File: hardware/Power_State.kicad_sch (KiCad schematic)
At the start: 27 parts, among them J12 Battery_Meas, J13 ICSP_Header_2, J14 5V_In, J15 Stat_LED, J16 ICSP_Header_1, J17 Button_Header, J18 RPI_POWER, Q2 AOD4184A, SW1 SW_DIP_x01, SW2 SW_Reset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

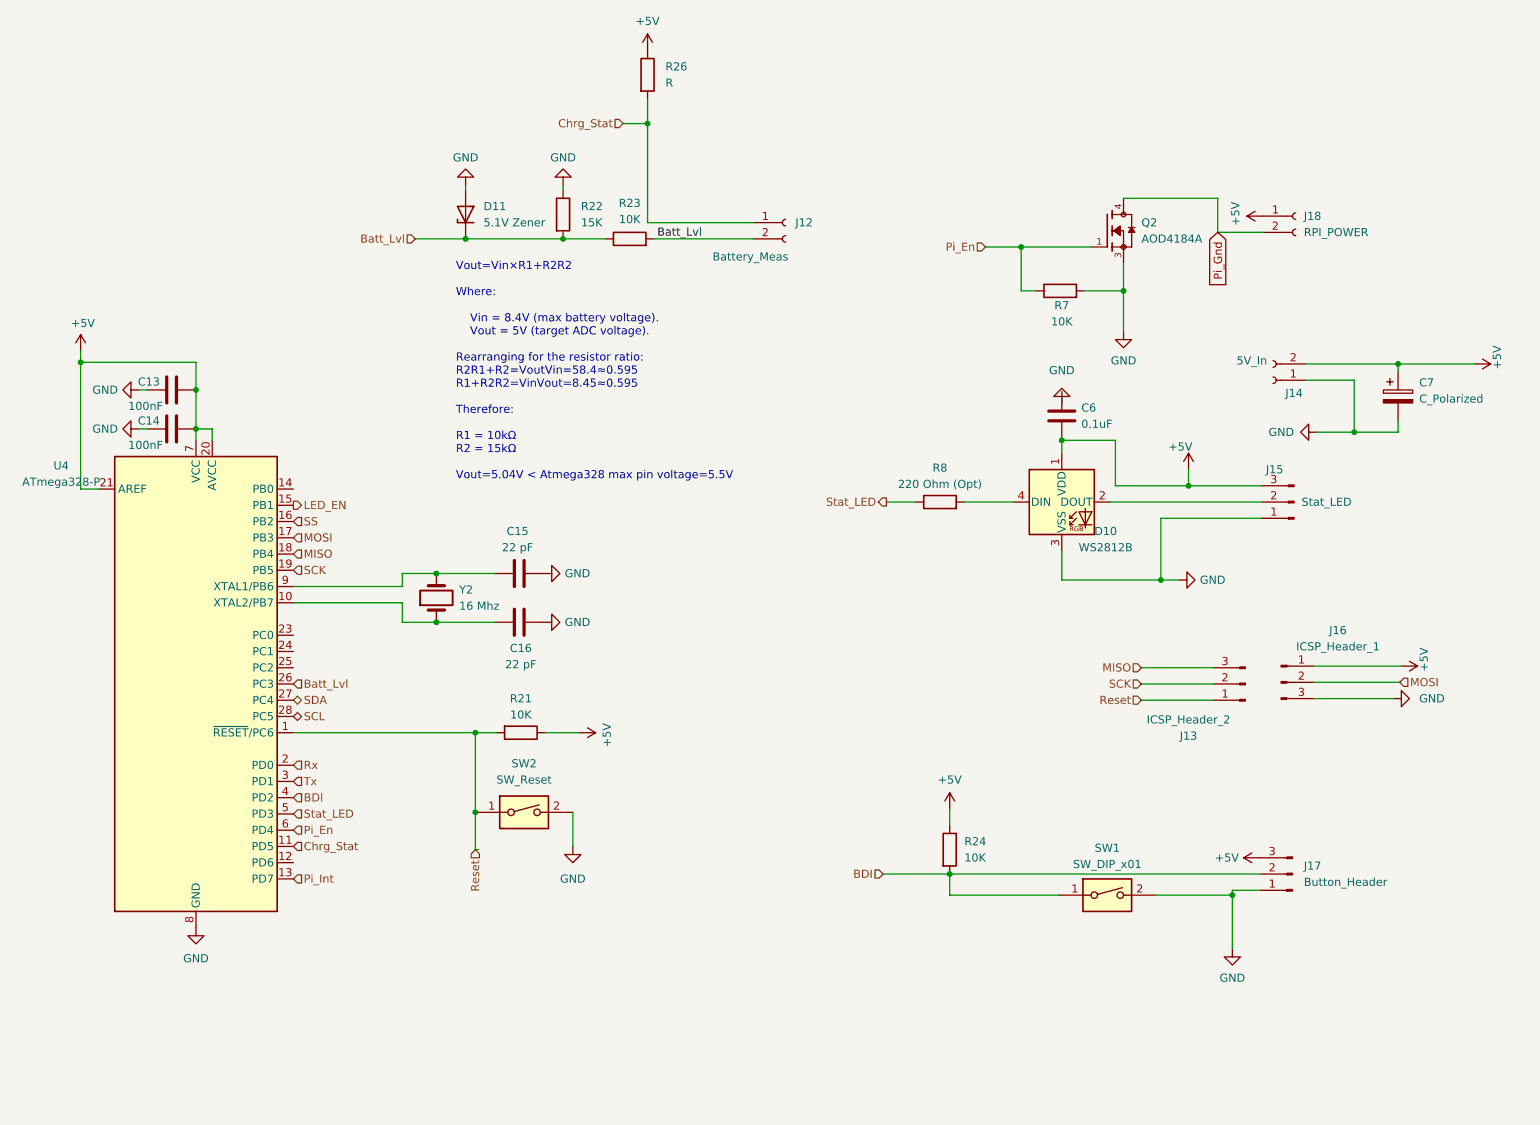
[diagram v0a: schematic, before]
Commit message: Hardware V0.2 - Schematics update
Combines Cell holder, BMS, and voltage regulator into single board
complete w. extensive electrical and thermal protections including:

* MM3220 BMS w Overvoltage, Overcurrent, undervoltage charging/discharge protect
* Fuses on cells, 12v in, 5v and 8.4v out.
* Reverse polarity protection on 12v and cells.

Adds debug UART header
Single IO header on every board
Minor component size corrections
Add current limiting resistor to RPI power NMOS gate.
Add optional support for MLCC/tantalum caps for Voltage Regulator instead of electrolytic
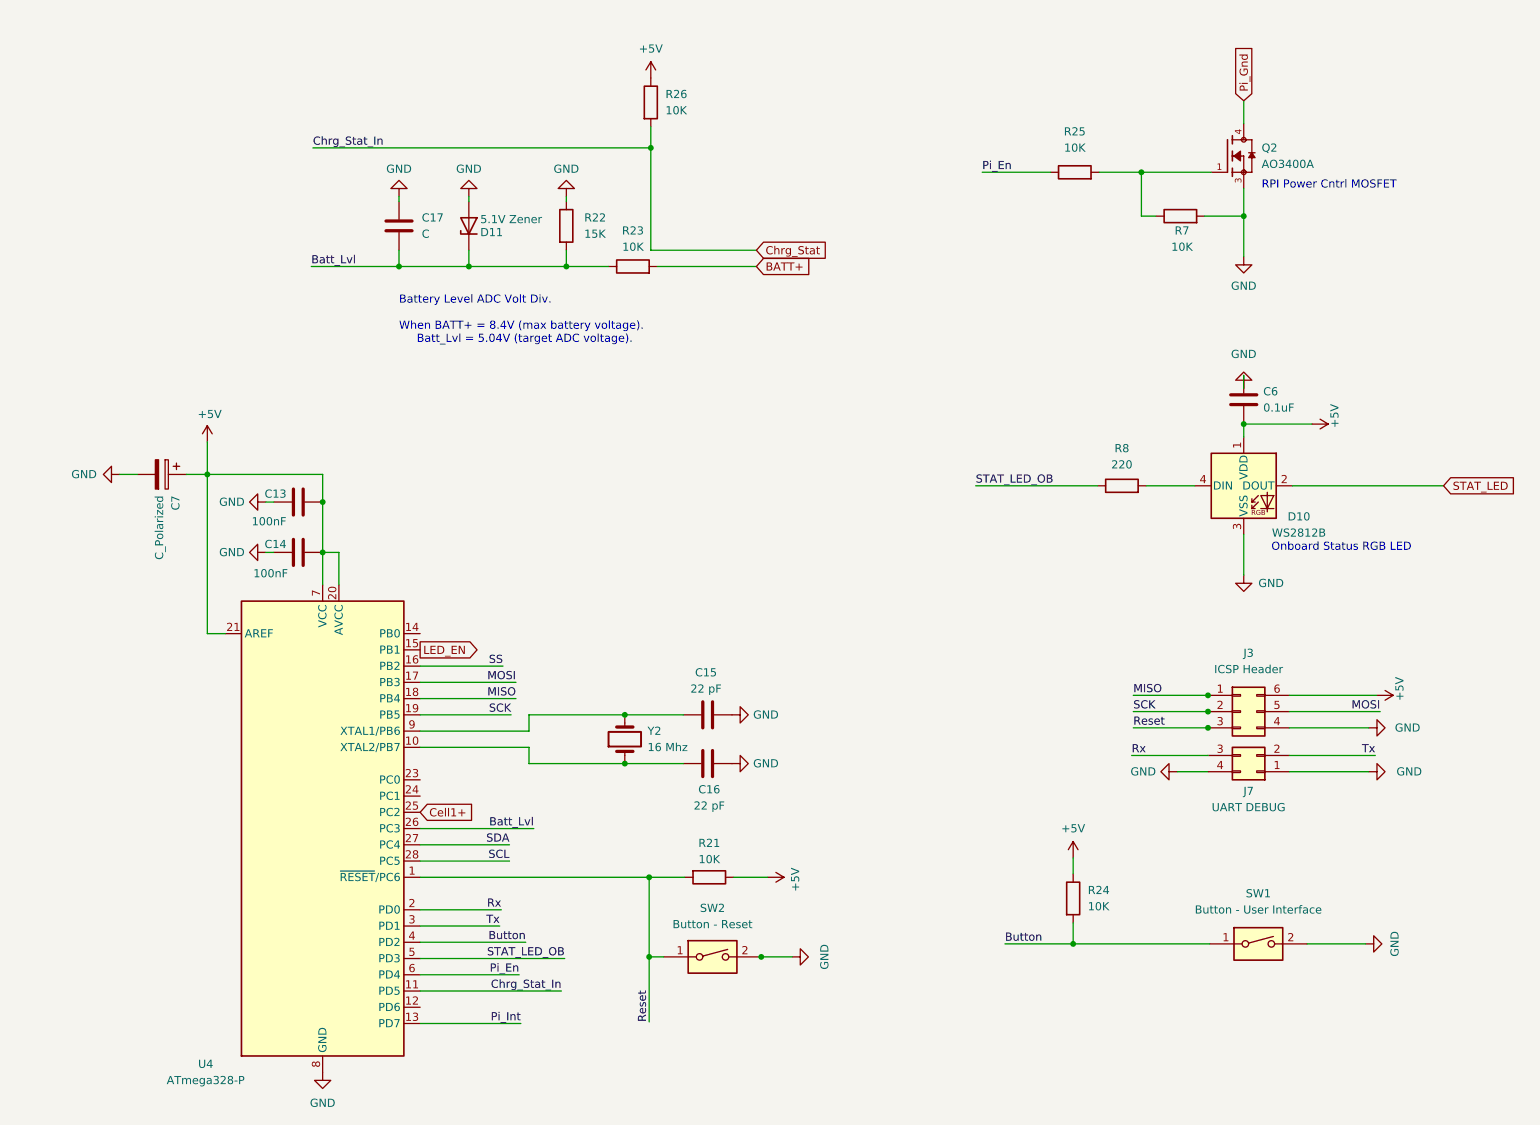
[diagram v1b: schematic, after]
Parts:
- removed J12: Battery_Meas, Connector_PinSocket_2.54mm:PinSocket_1x03_P2.54mm_Vertical, symbol Connector:Conn_01x02_Socket
- removed J13: ICSP_Header_2, Connector_PinSocket_2.54mm:PinSocket_1x03_P2.54mm_Vertical, symbol Connector:Conn_01x03_Pin
- removed J14: 5V_In, Connector_PinSocket_2.54mm:PinSocket_1x02_P2.54mm_Vertical, symbol Connector:Conn_01x02_Socket
- removed J15: Stat_LED, Connector_PinSocket_2.54mm:PinSocket_1x03_P2.54mm_Vertical, symbol Connector:Conn_01x03_Pin
- removed J16: ICSP_Header_1, Connector_PinSocket_2.54mm:PinSocket_1x03_P2.54mm_Vertical, symbol Connector:Conn_01x03_Pin
- removed J17: Button_Header, Connector_PinSocket_2.54mm:PinSocket_1x03_P2.54mm_Vertical, symbol Connector:Conn_01x03_Pin
- removed J18: RPI_POWER, Connector_PinSocket_2.54mm:PinSocket_1x02_P2.54mm_Vertical, symbol Connector:Conn_01x02_Socket
- added C17: C, Capacitor_SMD:C_0603_1608Metric_Pad1.08x0.95mm_HandSolder, symbol Device:C
- added J3: ICSP Header, Connector_PinSocket_2.54mm:PinSocket_2x03_P2.54mm_Vertical, symbol Connector_Generic:Conn_02x03_Counter_Clockwise
- added J7: UART DEBUG, Connector_PinSocket_2.54mm:PinSocket_2x02_P2.54mm_Vertical, symbol Connector_Generic:Conn_02x02_Counter_Clockwise
- added R25: 10K, Resistor_SMD:R_0603_1608Metric, symbol Device:R
- C13, C14, C15, C16, C6: footprint Capacitor_SMD:C_0504_1310Metric_Pad0.83x1.28mm_HandSolder -> Capacitor_SMD:C_0603_1608Metric_Pad1.08x0.95mm_HandSolder
- C7: footprint Capacitor_SMD:CP_Elec_6.3x5.9 -> Capacitor_SMD:C_0603_1608Metric_Pad1.08x0.95mm_HandSolder
- D11: footprint Diode_SMD:D_SC-80_HandSoldering -> Diode_SMD:D_MiniMELF_Handsoldering
- Q2: value AOD4184A -> AO3400A; footprint AOD4184A:DPAK228P994X240-4N -> FET - SI4435FDY:SO-8_VIS
- R26: value R -> 10K; footprint Resistor_SMD:R_0603_1608Metric_Pad0.98x0.95mm_HandSolder -> Resistor_SMD:R_0603_1608Metric
- R8: value 220 Ohm (Opt) -> 220
- SW1: value SW_DIP_x01 -> Button - User Interface
- SW2: value SW_Reset -> Button - Reset
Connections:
- net +5V: now also J3.6 (Pin_6)
- net Batt_Lvl: now also C17.2; no longer R23.2
- net GND: now also C17.1, J3.4 (Pin_4), J7.1 (Pin_1), J7.4 (Pin_4)
- net MISO: now also J3.1 (Pin_1)
- net MOSI: now also J3.5 (Pin_5)
- net Pi_En: now also R25.1; no longer Q2.1, R7.1
- net Reset: now also J3.3 (Pin_3)
- net Rx: now also J7.3 (Pin_3)
- net SCK: now also J3.2 (Pin_2)
- net Tx: now also J7.2 (Pin_2)
- net STAT_LED: now reaches D10.2 (DOUT)
- net Cell1+: now reaches U4.25 (PC2)
- net BDI renamed Button
- net Stat_LED renamed STAT_LED_OB
- new net: Q2.1, R25.2, R7.1
- new net BATT+: R23.2
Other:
- note added: "Battery Level ADC Volt Div. When BATT+ = 8.4V (max battery voltage). Batt_Lvl = 5.04V (target ADC voltage)."
- note added: "Onboard Status RGB LED"
- note added: "RPI Power Cntrl MOSFET"
- note removed: "Vout​=Vin​×R1+R2R2​ Where: Vin = 8.4V (max battery voltage). Vout = 5V (target ADC voltage). Rearranging for the resistor ratio: R2R1+R2=VoutVin=58.4≈0.595 R1+R2R2​=Vin​Vout​​=8.45​≈0.595 Therefore: R1 = 10kΩ R2 = 15kΩ Vout=5.04V < Atmega328 max pin voltage=5.5V"
- moved on the sheet: C13, C14, C15, C16, C6, C7, D10, D11, Q2, R21, R22, R23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

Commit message: Hardware revision 0.2 routing
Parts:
- removed C7: C_Polarized, Capacitor_SMD:C_0603_1608Metric_Pad1.08x0.95mm_HandSolder, symbol Device:C_Polarized
- removed Q2: AO3400A, FET - SI4435FDY:SO-8_VIS, symbol AOD4184A:AOD4184A
- added C7: 47uF 1210, Capacitor_SMD:C_1210_3225Metric_Pad1.33x2.70mm_HandSolder, symbol Device:C
- added Q2: NMOS, FET - AOSP36326C:SOIC127P490X600X175-8N, symbol Simulation_SPICE:NMOS
- C17: value C -> 100nF
- SW1, SW2: footprint Buttons:Button_Sw_THT -> Button - PTS815 Tactile SW:SW4_PTS815 SJM 250 SMTR LFS_CNK
- U4: footprint Package_DIP:DIP-28_W7.62mm -> ATMEGA328-AU:QFP80P900X900X120-32N
- Y2: footprint Crystal:Crystal_HC49-U_Vertical -> Crystal - 16MHz ECS_160_20_5PX_TR:XTAL_ECS-160-20-5PX-TR
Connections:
- net +5V: now also C7.2
- net GND: now also C7.1, Q2.3 (S)
- net Pi_Gnd: now also Q2.1 (D)
- net at R25.2, R7.1: now also Q2.2 (G)
- net BATT+ renamed 8.4V
- net Cell1+ renamed BATT_LVL_MID
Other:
- company: (none) -> KBader94
- title: (none) -> OpenActionCam
- moved on the sheet: C17
